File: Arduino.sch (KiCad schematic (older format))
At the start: 0 parts

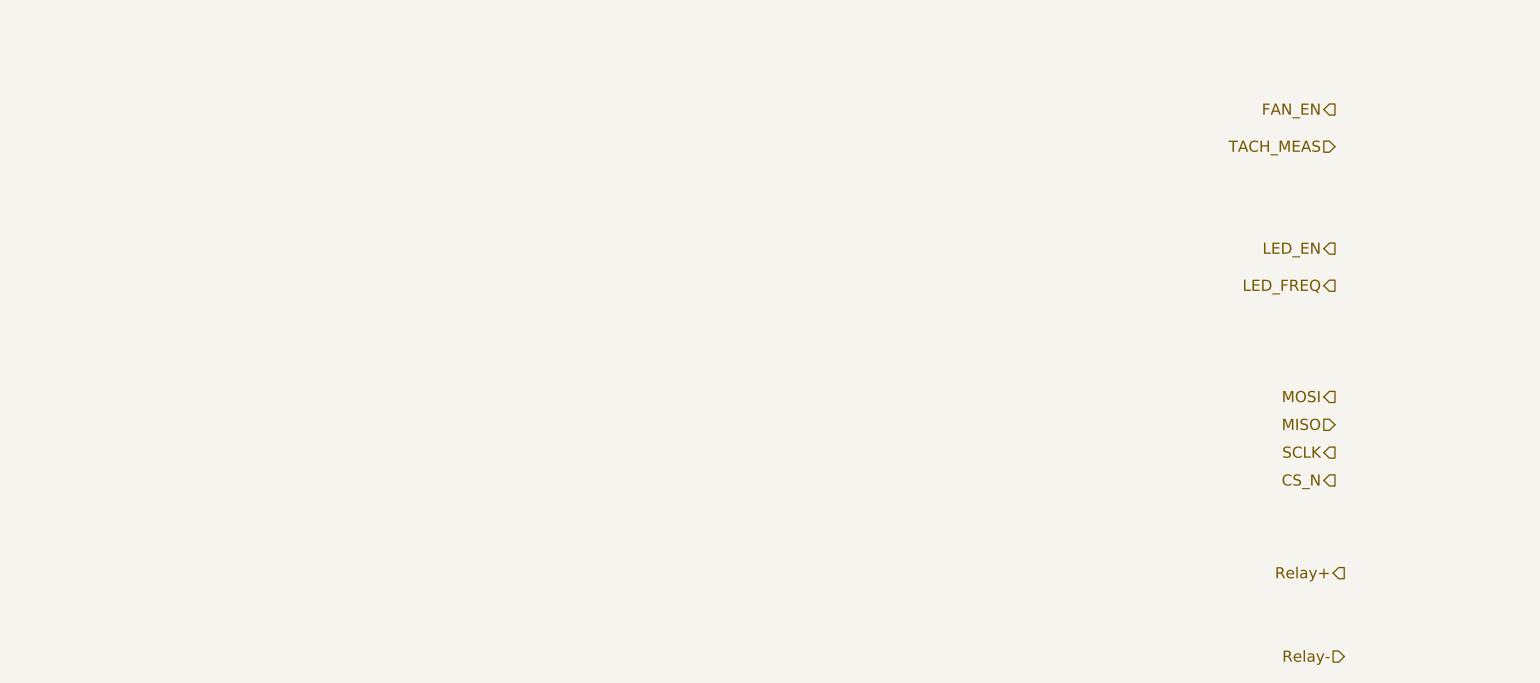
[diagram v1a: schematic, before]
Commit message: Current driver refactoring, LED module, Arduino
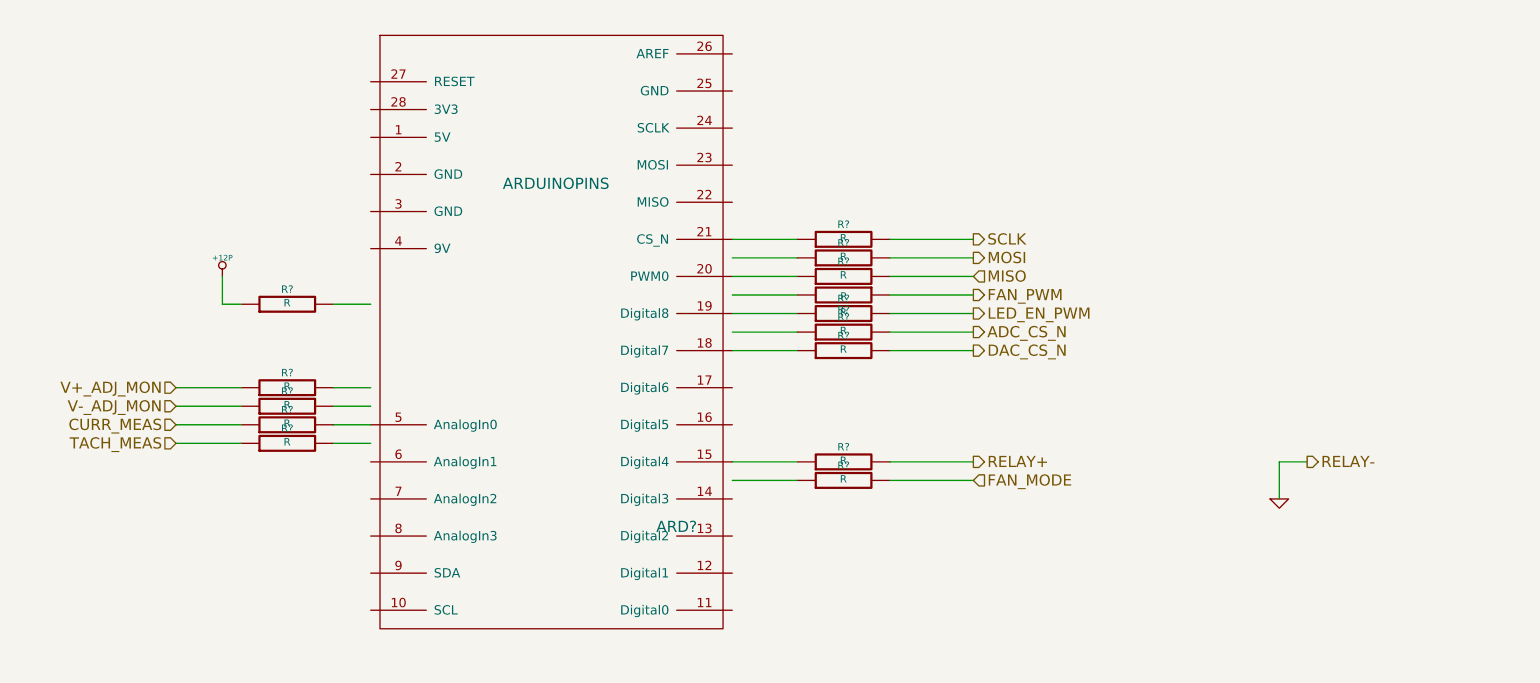
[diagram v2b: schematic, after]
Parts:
- added ARD?: ARDUINOPINS, symbol ARDUINOPINS
- added R? (x14): R, ~, symbol R
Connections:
- net labels added: +12P, ADC_CS_N, CURR_MEAS, DAC_CS_N, FAN_MODE, FAN_PWM, GND, LED_EN_PWM, RELAY+, RELAY-, V+_ADJ_MON, V-_ADJ_MON
- net labels removed: CS_N, FAN_EN, LED_EN, LED_FREQ, Relay+, Relay-
- wire segments 0 -> 31

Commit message: Refactoring and Created key shortcuts
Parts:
- added R? (x4): R, ~, symbol R
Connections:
- net labels added: +5V
- wire segments 31 -> 40
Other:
- moved on the sheet: R?

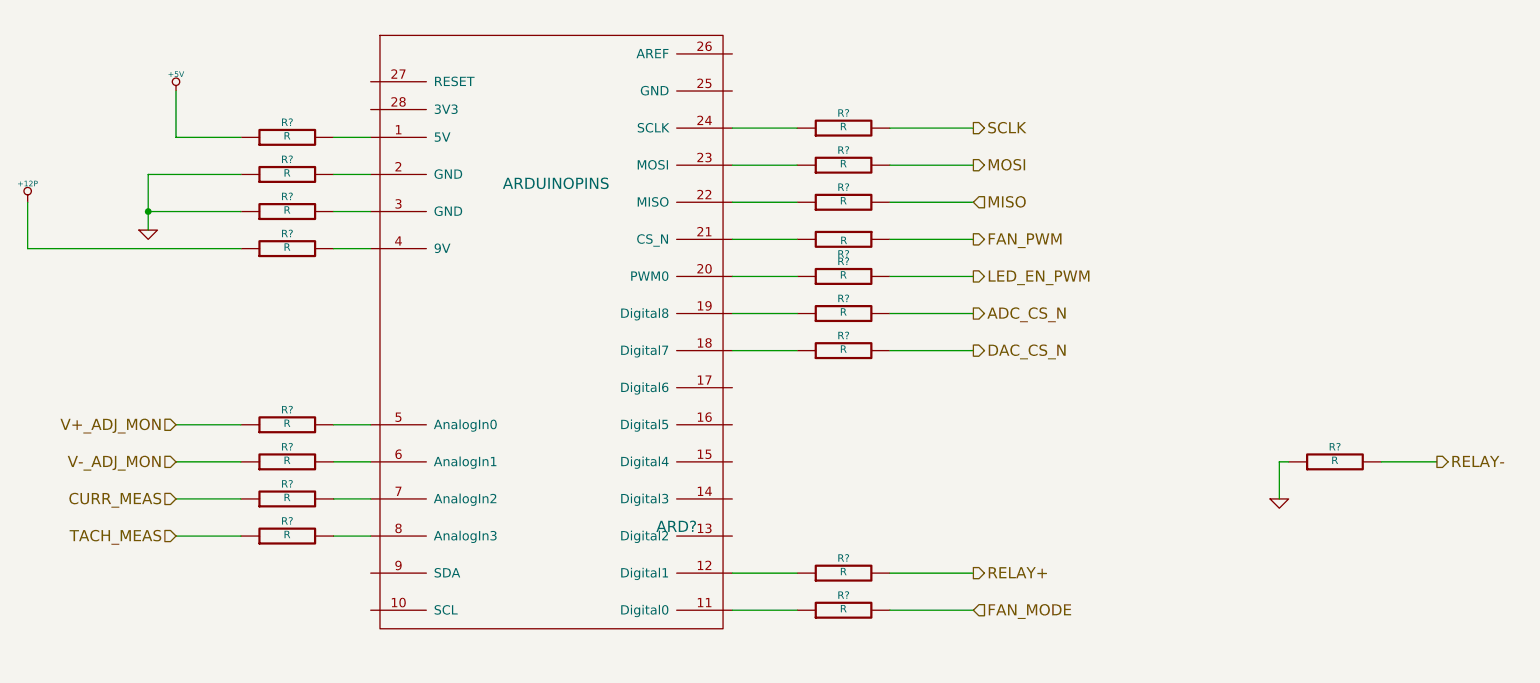
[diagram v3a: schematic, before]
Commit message: Relay module association and placement
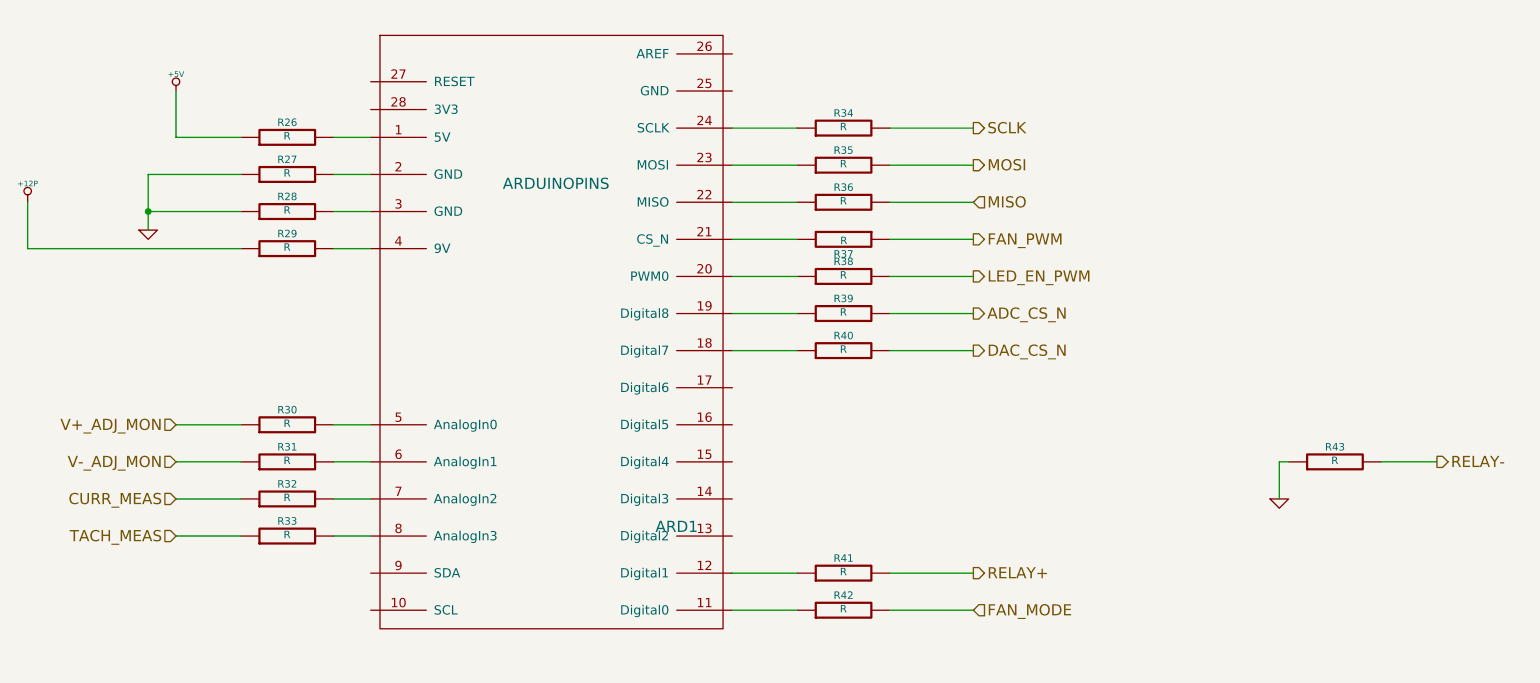
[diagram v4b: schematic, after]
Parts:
- gave numbers to parts that had none: 19
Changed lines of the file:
@@
 Sheet 9 9
 Title ""
-Date "18 feb 2014"
+Date "20 feb 2014"
 Rev ""
 Comp ""
@@
 TACH_MEAS
 $Comp
-L ARDUINOPINS ARD?
+L ARDUINOPINS ARD1
 U 1 1 52F8718B
 P 4050 4000
-F 0 "ARD?" H 4750 3050 60  0000 C CNN
+F 0 "ARD1" H 4750 3050 60  0000 C CNN
 F 1 "ARDUINOPINS" H 4100 4900 60  0000 C CNN
 F 2 "" H 4100 2700 60  0000 C CNN
@@
 CURR_MEAS
 $Comp
-L R R?
+L R R37
 U 1 1 52F874A4
 P 5650 3400
-F 0 "R?" V 5730 3400 40  0000 C CNN
+F 0 "R37" V 5730 3400 40  0000 C CNN
 F 1 "R" V 5657 3401 40  0000 C CNN
 F 2 "~" V 5580 3400 30  0000 C CNN
@@
 	5900 3400 6350 3400
 $Comp
-L R R?
+L R R41
 U 1 1 52F874CB
 P 5650 5200
-F 0 "R?" V 5730 5200 40  0000 C CNN
+F 0 "R41" V 5730 5200 40  0000 C CNN
 F 1 "R" V 5657 5201 40  0000 C CNN
 F 2 "~" V 5580 5200 30  0000 C CNN
@@
 	5900 5200 6350 5200
 $Comp
-L GND #PWR?
+L GND #PWR047
 U 1 1 52F88224
 P 8000 4800
-F 0 "#PWR?" H 8000 4800 30  0001 C CNN
+F 0 "#PWR047" H 8000 4800 30  0001 C CNN
 F 1 "GND" H 8000 4730 30  0001 C CNN
 F 2 "" H 8000 4800 60  0000 C CNN
@@
 	8000 4800 8000 4600
 $Comp
-L R R?
+L R R33
 U 1 1 52F8823A
 P 2650 5000
-F 0 "R?" V 2730 5000 40  0000 C CNN
+F 0 "R33" V 2730 5000 40  0000 C CNN
 F 1 "R" V 2657 5001 40  0000 C CNN
 F 2 "~" V 2580 5000 30  0000 C CNN
@@
 $EndComp
 $Comp
-L R R?
+L R R32
 U 1 1 52F88240
 P 2650 4800
-F 0 "R?" V 2730 4800 40  0000 C CNN
+F 0 "R32" V 2730 4800 40  0000 C CNN
 F 1 "R" V 2657 4801 40  0000 C CNN
 F 2 "~" V 2580 4800 30  0000 C CNN
@@
 V-_ADJ_MON
 $Comp
-L R R?
+L R R31
 U 1 1 52F88E4E
 P 2650 4600
-F 0 "R?" V 2730 4600 40  0000 C CNN
+F 0 "R31" V 2730 4600 40  0000 C CNN
 F 1 "R" V 2657 4601 40  0000 C CNN
 F 2 "~" V 2580 4600 30  0000 C CNN
@@
 $EndComp
 $Comp
-L R R?
+L R R30
 U 1 1 52F88E54
 P 2650 4400
-F 0 "R?" V 2730 4400 40  0000 C CNN
+F 0 "R30" V 2730 4400 40  0000 C CNN
 F 1 "R" V 2657 4401 40  0000 C CNN
 F 2 "~" V 2580 4400 30  0000 C CNN
@@
 	3100 4600 2900 4600
 $Comp
-L R R?
+L R R40
 U 1 1 52F88E9C
 P 5650 4000
-F 0 "R?" V 5730 4000 40  0000 C CNN
+F 0 "R40" V 5730 4000 40  0000 C CNN
 F 1 "R" V 5657 4001 40  0000 C CNN
 F 2 "~" V 5580 4000 30  0000 C CNN
@@
 $EndComp
 $Comp
-L R R?
+L R R36
 U 1 1 52F88EA2
 P 5650 3200
-F 0 "R?" V 5730 3200 40  0000 C CNN
+F 0 "R36" V 5730 3200 40  0000 C CNN
 F 1 "R" V 5657 3201 40  0000 C CNN
 F 2 "~" V 5580 3200 30  0000 C CNN
@@
 $EndComp
 $Comp
-L R R?
+L R R35
 U 1 1 52F88EA8
 P 5650 3000
-F 0 "R?" V 5730 3000 40  0000 C CNN
+F 0 "R35" V 5730 3000 40  0000 C CNN
 F 1 "R" V 5657 3001 40  0000 C CNN
 F 2 "~" V 5580 3000 30  0000 C CNN
@@
 $EndComp
 $Comp
-L R R?
+L R R34
 U 1 1 52F88EAE
 P 5650 2800
-F 0 "R?" V 5730 2800 40  0000 C CNN
+F 0 "R34" V 5730 2800 40  0000 C CNN
 F 1 "R" V 5657 2801 40  0000 C CNN
 F 2 "~" V 5580 2800 30  0000 C CNN
@@
 LED_EN_PWM
 $Comp
-L R R?
+L R R38
 U 1 1 52F88F48
 P 5650 3600
-F 0 "R?" V 5730 3600 40  0000 C CNN
+F 0 "R38" V 5730 3600 40  0000 C CNN
 F 1 "R" V 5657 3601 40  0000 C CNN
 F 2 "~" V 5580 3600 30  0000 C CNN
@@
 	5900 3600 6350 3600
 $Comp
-L R R?
+L R R39
 U 1 1 52F8F934
 P 5650 3800
-F 0 "R?" V 5730 3800 40  0000 C CNN
+F 0 "R39" V 5730 3800 40  0000 C CNN
 F 1 "R" V 5657 3801 40  0000 C CNN
 F 2 "~" V 5580 3800 30  0000 C CNN
@@
 FAN_MODE
 $Comp
-L R R?
+L R R42
 U 1 1 52F7EF78
 P 5650 5400
-F 0 "R?" V 5730 5400 40  0000 C CNN
+F 0 "R42" V 5730 5400 40  0000 C CNN
 F 1 "R" V 5657 5401 40  0000 C CNN
 F 2 "~" V 5580 5400 30  0000 C CNN
@@
 	5050 5400 5400 5400
 $Comp
-L R R?
+L R R29
 U 1 1 52F7F221
 P 2650 3450
-F 0 "R?" V 2730 3450 40  0000 C CNN
+F 0 "R29" V 2730 3450 40  0000 C CNN
 F 1 "R" V 2657 3451 40  0000 C CNN
 F 2 "~" V 2580 3450 30  0000 C CNN
@@
 	2900 3450 3100 3450
 $Comp
-L +12P #PWR?
+L +12P #PWR048
 U 1 1 52F7F246
 P 1250 3200
-F 0 "#PWR?" H 1250 3170 30  0001 C CNN
+F 0 "#PWR048" H 1250 3170 30  0001 C CNN
 F 1 "+12P" H 1250 3300 30  0000 C CNN
 F 2 "" H 1250 3200 60  0000 C CNN
@@
 	1250 3200 1250 3450
 $Comp
-L R R?
+L R R28
 U 1 1 5302C571
 P 2650 3250
-F 0 "R?" V 2730 3250 40  0000 C CNN
+F 0 "R28" V 2730 3250 40  0000 C CNN
 F 1 "R" V 2657 3251 40  0000 C CNN
 F 2 "~" V 2580 3250 30  0000 C CNN
@@
 $EndComp
 $Comp
-L R R?
+L R R27
 U 1 1 5302C577
 P 2650 3050
-F 0 "R?" V 2730 3050 40  0000 C CNN
+F 0 "R27" V 2730 3050 40  0000 C CNN
 F 1 "R" V 2657 3051 40  0000 C CNN
 F 2 "~" V 2580 3050 30  0000 C CNN
@@
 $EndComp
 $Comp
-L R R?
+L R R26
 U 1 1 5302C57D
 P 2650 2850
-F 0 "R?" V 2730 2850 40  0000 C CNN
+F 0 "R26" V 2730 2850 40  0000 C CNN
 F 1 "R" V 2657 2851 40  0000 C CNN
 F 2 "~" V 2580 2850 30  0000 C CNN
@@
 	2900 3250 3100 3250
 $Comp
-L GND #PWR?
+L GND #PWR049
 U 1 1 5302C5E6
 P 1900 3350
-F 0 "#PWR?" H 1900 3350 30  0001 C CNN
+F 0 "#PWR049" H 1900 3350 30  0001 C CNN
 F 1 "GND" H 1900 3280 30  0001 C CNN
 F 2 "" H 1900 3350 60  0000 C CNN
@@
 Connection ~ 1900 3250
 $Comp
-L +5V #PWR?
+L +5V #PWR050
 U 1 1 5302C682
 P 2050 2600
-F 0 "#PWR?" H 2050 2690 20  0001 C CNN
+F 0 "#PWR050" H 2050 2690 20  0001 C CNN
 F 1 "+5V" H 2050 2690 30  0000 C CNN
 F 2 "" H 2050 2600 60  0000 C CNN
@@
 	2050 2850 2400 2850
 $Comp
-L R R?
+L R R43
 U 1 1 5302C91F
 P 8300 4600
-F 0 "R?" V 8380 4600 40  0000 C CNN
+F 0 "R43" V 8380 4600 40  0000 C CNN
 F 1 "R" V 8307 4601 40  0000 C CNN
 F 2 "~" V 8230 4600 30  0000 C CNN

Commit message: Thermocouple association and placement
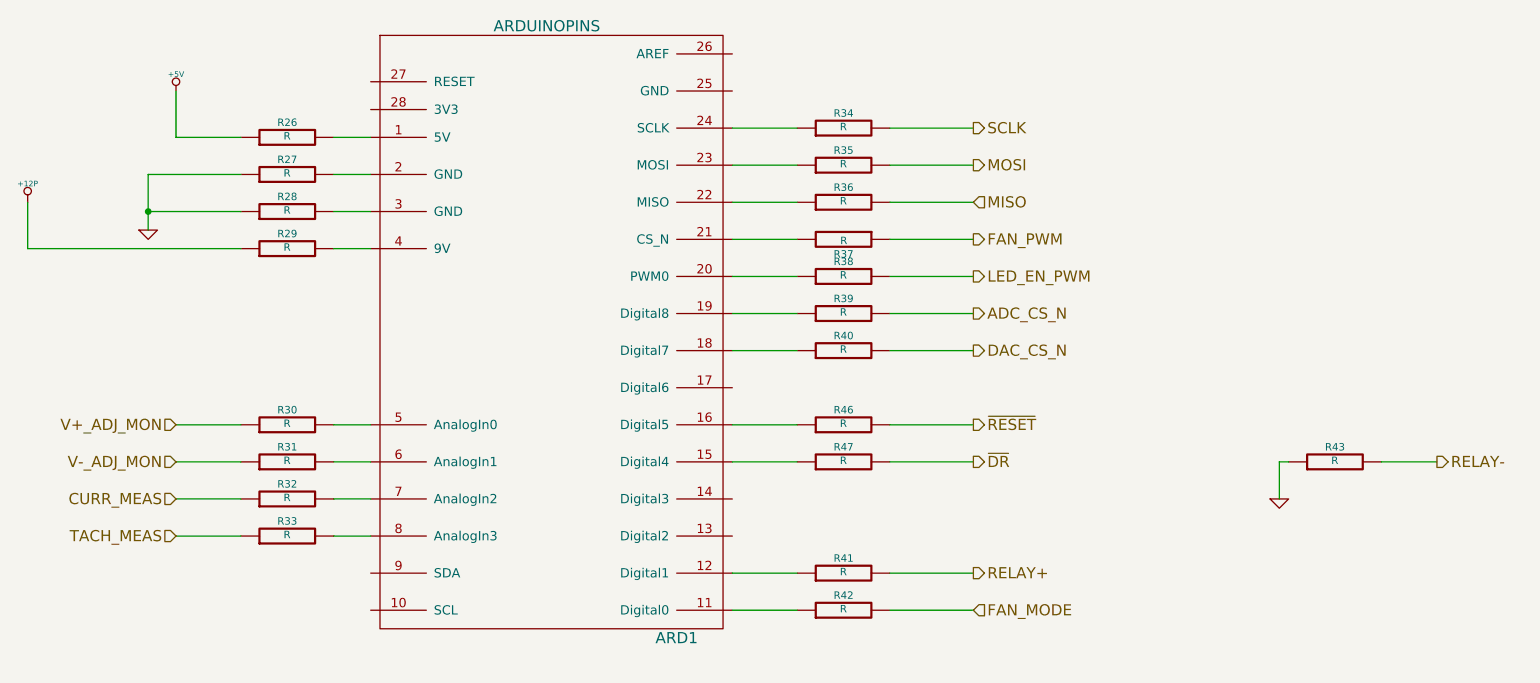
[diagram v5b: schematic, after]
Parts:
- added R46, R47: R, ~, symbol R
- ARD1: footprint (none) -> ~
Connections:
- net at ARD1.15 (Digital4): now also R47.1
- net at ARD1.16 (Digital5): now also R46.1
- new net ~DR: R47.2
- new net ~RESET: R46.2
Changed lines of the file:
@@
 $Descr A4 11693 8268
 encoding utf-8
-Sheet 9 9
+Sheet 7 9
 Title ""
-Date "20 feb 2014"
+Date "21 feb 2014"
 Rev ""
 Comp ""
@@
 Text HLabel 2050 5000 0    60   Input ~ 0
 TACH_MEAS
-$Comp
-L ARDUINOPINS ARD1
-U 1 1 52F8718B
-P 4050 4000
-F 0 "ARD1" H 4750 3050 60  0000 C CNN
-F 1 "ARDUINOPINS" H 4100 4900 60  0000 C CNN
-F 2 "" H 4100 2700 60  0000 C CNN
-F 3 "" H 4100 2700 60  0000 C CNN
-	1    4050 4000
-	1    0    0    -1
-$EndComp
 Text HLabel 2050 4800 0    60   Input ~ 0
 CURR_MEAS
@@
 	5900 5200 6350 5200
 $Comp
-L GND #PWR047
+L GND #PWR43
 U 1 1 52F88224
 P 8000 4800
-F 0 "#PWR047" H 8000 4800 30  0001 C CNN
+F 0 "#PWR43" H 8000 4800 30  0001 C CNN
 F 1 "GND" H 8000 4730 30  0001 C CNN
 F 2 "" H 8000 4800 60  0000 C CNN
@@
 	2900 3450 3100 3450
 $Comp
-L +12P #PWR048
+L +12P #PWR40
 U 1 1 52F7F246
 P 1250 3200
-F 0 "#PWR048" H 1250 3170 30  0001 C CNN
+F 0 "#PWR40" H 1250 3170 30  0001 C CNN
 F 1 "+12P" H 1250 3300 30  0000 C CNN
 F 2 "" H 1250 3200 60  0000 C CNN
@@
 	2900 3250 3100 3250
 $Comp
-L GND #PWR049
+L GND #PWR41
 U 1 1 5302C5E6
 P 1900 3350
-F 0 "#PWR049" H 1900 3350 30  0001 C CNN
+F 0 "#PWR41" H 1900 3350 30  0001 C CNN
 F 1 "GND" H 1900 3280 30  0001 C CNN
 F 2 "" H 1900 3350 60  0000 C CNN
@@
 Connection ~ 1900 3250
 $Comp
-L +5V #PWR050
+L +5V #PWR42
 U 1 1 5302C682
 P 2050 2600
-F 0 "#PWR050" H 2050 2690 20  0001 C CNN
+F 0 "#PWR42" H 2050 2690 20  0001 C CNN
 F 1 "+5V" H 2050 2690 30  0000 C CNN
 F 2 "" H 2050 2600 60  0000 C CNN
@@
 Wire Wire Line
 	8550 4600 8850 4600
+Text HLabel 6350 4400 2    60   Output ~ 0
+~RESET
+$Comp
+L R R46
+U 1 1 53070C68
+P 5650 4400
+F 0 "R46" V 5730 4400 40  0000 C CNN
+F 1 "R" V 5657 4401 40  0000 C CNN
+F 2 "~" V 5580 4400 30  0000 C CNN
+F 3 "~" H 5650 4400 30  0000 C CNN
+	1    5650 4400
+	0    -1   -1   0
+$EndComp
+Wire Wire Line
+	5400 4400 5050 4400
+Wire Wire Line
+	5900 4400 6350 4400
+Text HLabel 6350 4600 2    60   Output ~ 0
+~DR
+$Comp
+L R R47
+U 1 1 53070C71
+P 5650 4600
+F 0 "R47" V 5730 4600 40  0000 C CNN
+F 1 "R" V 5657 4601 40  0000 C CNN
+F 2 "~" V 5580 4600 30  0000 C CNN
+F 3 "~" H 5650 4600 30  0000 C CNN
+	1    5650 4600
+	0    -1   -1   0
+$EndComp
+Wire Wire Line
+	5400 4600 5050 4600
+Wire Wire Line
+	5900 4600 6350 4600
+$Comp
+L ARDUINOPINS ARD1
+U 1 1 53070C98
+P 4050 4000
+F 0 "ARD1" H 4750 2450 60  0000 C CNN
+F 1 "ARDUINOPINS" H 4050 5750 60  0000 C CNN
+F 2 "~" H 4100 2500 60  0000 C CNN
+F 3 "~" H 4100 2500 60  0000 C CNN
+	1    4050 4000
+	1    0    0    -1
+$EndComp
 $EndSCHEMATC
